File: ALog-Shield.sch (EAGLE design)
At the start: 25 parts, among them U1 DS3231MZ/V+T

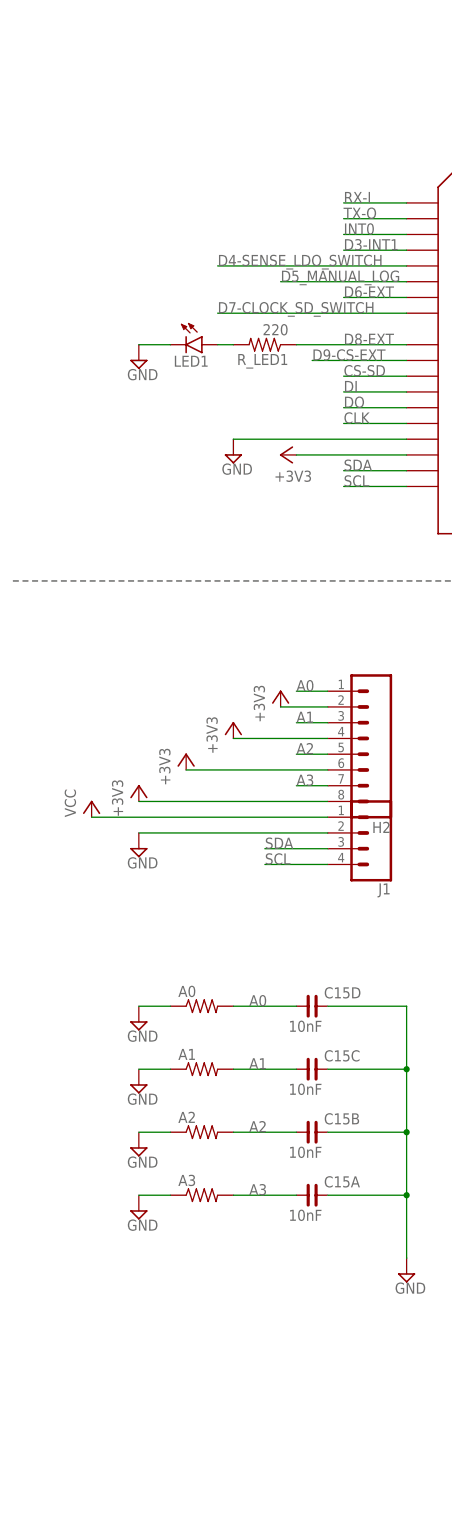
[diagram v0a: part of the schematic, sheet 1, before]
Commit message: ALog and Made in MN back silk
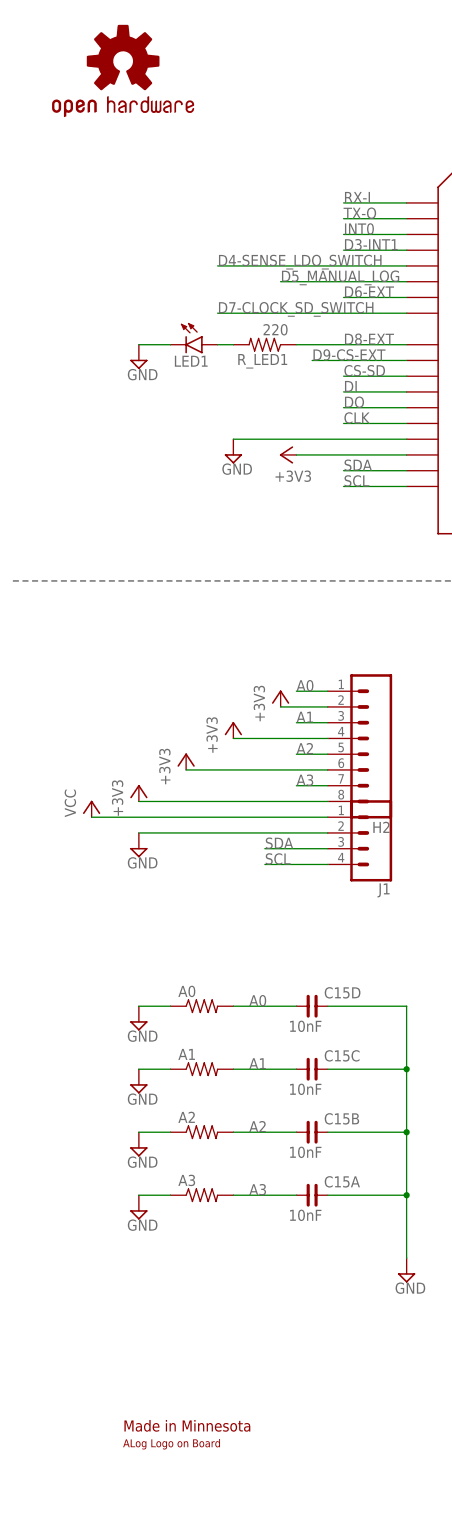
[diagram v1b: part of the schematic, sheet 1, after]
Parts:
- removed U$1: ALOG_LOGO_V1_5.5MM, awickert:ALOG_LOGO_V1_5.5MM
- removed U$4: NWLOGO, awickert:NWLOGO
- added LOGO1: OSHW-LOGOL, SparkFun-Aesthetics:OSHW-LOGOL
- added U$2: MADE_IN_MN_220_SHIELD, awickert:MADE_IN_MN_220_SHIELD
- added U$3: ALOG_LOG, awickert:ALOG_LOG
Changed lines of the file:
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@@
 <part name="SUPPLY45" library="supply2" deviceset="GND" device=""/>
 <part name="R_LED1" library="resistor" deviceset="R-US_" device="R0603" value="220"/>
-<part name="U$1" library="awickert" deviceset="ALOG_LOGO_V1_5.5MM" device=""/>
 <part name="+3V13" library="supply1" deviceset="+3V3" device=""/>
 <part name="A1" library="resistor" deviceset="R-US_" device="0207/10"/>
 <part name="SUPPLY47" library="supply2" deviceset="GND" device=""/>
-<part name="U$4" library="awickert" deviceset="NWLOGO" device=""/>
 <part name="LOGO2" library="SparkFun-Aesthetics" deviceset="OSHW-LOGO" device="M"/>
 <part name="SUPPLY52" library="supply2" deviceset="GND" device=""/>
@@
 <part name="C15" library="rc-master-smd" deviceset="CCA_" device="" value="10nF"/>
 <part name="CLOCK_BATT" library="awickert" deviceset="LINX-BAT-HLD-012-SMT-OTL" device="" value="Linx BAT-HLD-012-SMT"/>
+<part name="U$2" library="awickert" deviceset="MADE_IN_MN_220_SHIELD" device=""/>
+<part name="U$3" library="awickert" deviceset="ALOG_LOG" device=""/>
+<part name="LOGO1" library="SparkFun-Aesthetics" deviceset="OSHW-LOGO" device="L"/>
 </parts>
 <sheets>
@@
 <instance part="C15" gate="C" x="48.26" y="-175.26"/>
 <instance part="C15" gate="D" x="48.26" y="-165.1"/>
+<instance part="U$2" gate="G$1" x="17.78" y="-233.68"/>
+<instance part="U$3" gate="G$1" x="25.4" y="-236.22"/>
+<instance part="LOGO1" gate="G$1" x="17.78" y="-12.7"/>
 </instances>
 <busses>
@@
 <instance part="SUPPLY36" gate="GND" x="93.98" y="106.68"/>
 <instance part="SUPPLY41" gate="GND" x="58.42" y="233.68"/>
-<instance part="U$1" gate="G$1" x="127" y="53.34"/>
-<instance part="U$4" gate="G$1" x="127" y="55.88"/>
 <instance part="LOGO2" gate="G$1" x="165.1" y="60.96"/>
 <instance part="CLOCK_BATT_DECOUP" gate="G$1" x="99.06" y="129.54" smashed="yes">

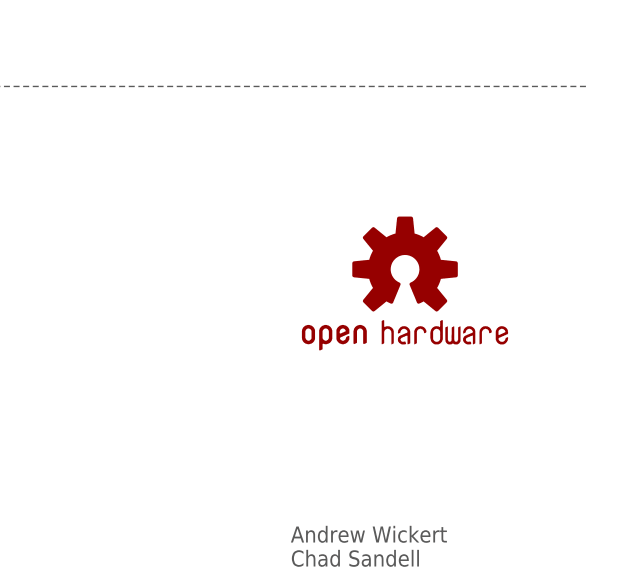
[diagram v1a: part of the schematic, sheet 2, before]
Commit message: Update silk and OSE logo
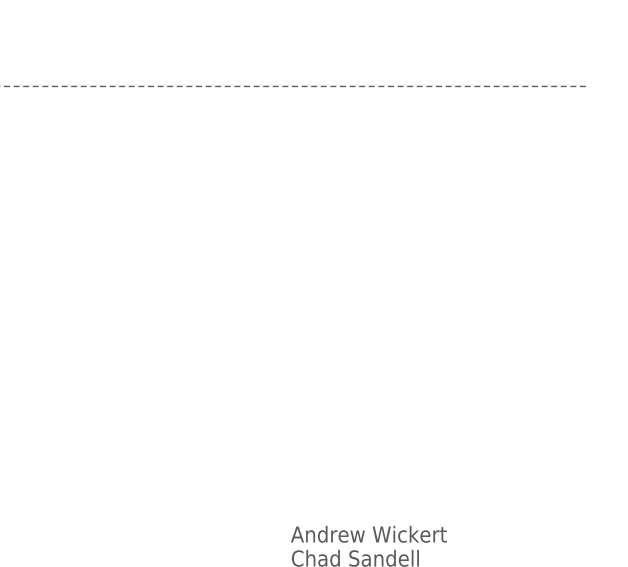
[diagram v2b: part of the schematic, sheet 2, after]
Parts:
- removed LOGO2: OSHW-LOGOM, SparkFun-Aesthetics:OSHW-LOGOM
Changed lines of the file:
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@@
 <part name="A1" library="resistor" deviceset="R-US_" device="0207/10"/>
 <part name="SUPPLY47" library="supply2" deviceset="GND" device=""/>
-<part name="LOGO2" library="SparkFun-Aesthetics" deviceset="OSHW-LOGO" device="M"/>
 <part name="SUPPLY52" library="supply2" deviceset="GND" device=""/>
 <part name="RESET" library="SparkFun-Electromechanical" deviceset="SWITCH-MOMENTARY-2" device="PTH" value="Reset"/>
@@
 <instance part="SUPPLY36" gate="GND" x="93.98" y="106.68"/>
 <instance part="SUPPLY41" gate="GND" x="58.42" y="233.68"/>
-<instance part="LOGO2" gate="G$1" x="165.1" y="60.96"/>
 <instance part="CLOCK_BATT_DECOUP" gate="G$1" x="99.06" y="129.54" smashed="yes">
 <attribute name="VALUE" x="100.584" y="124.841" size="1.778" layer="96"/>

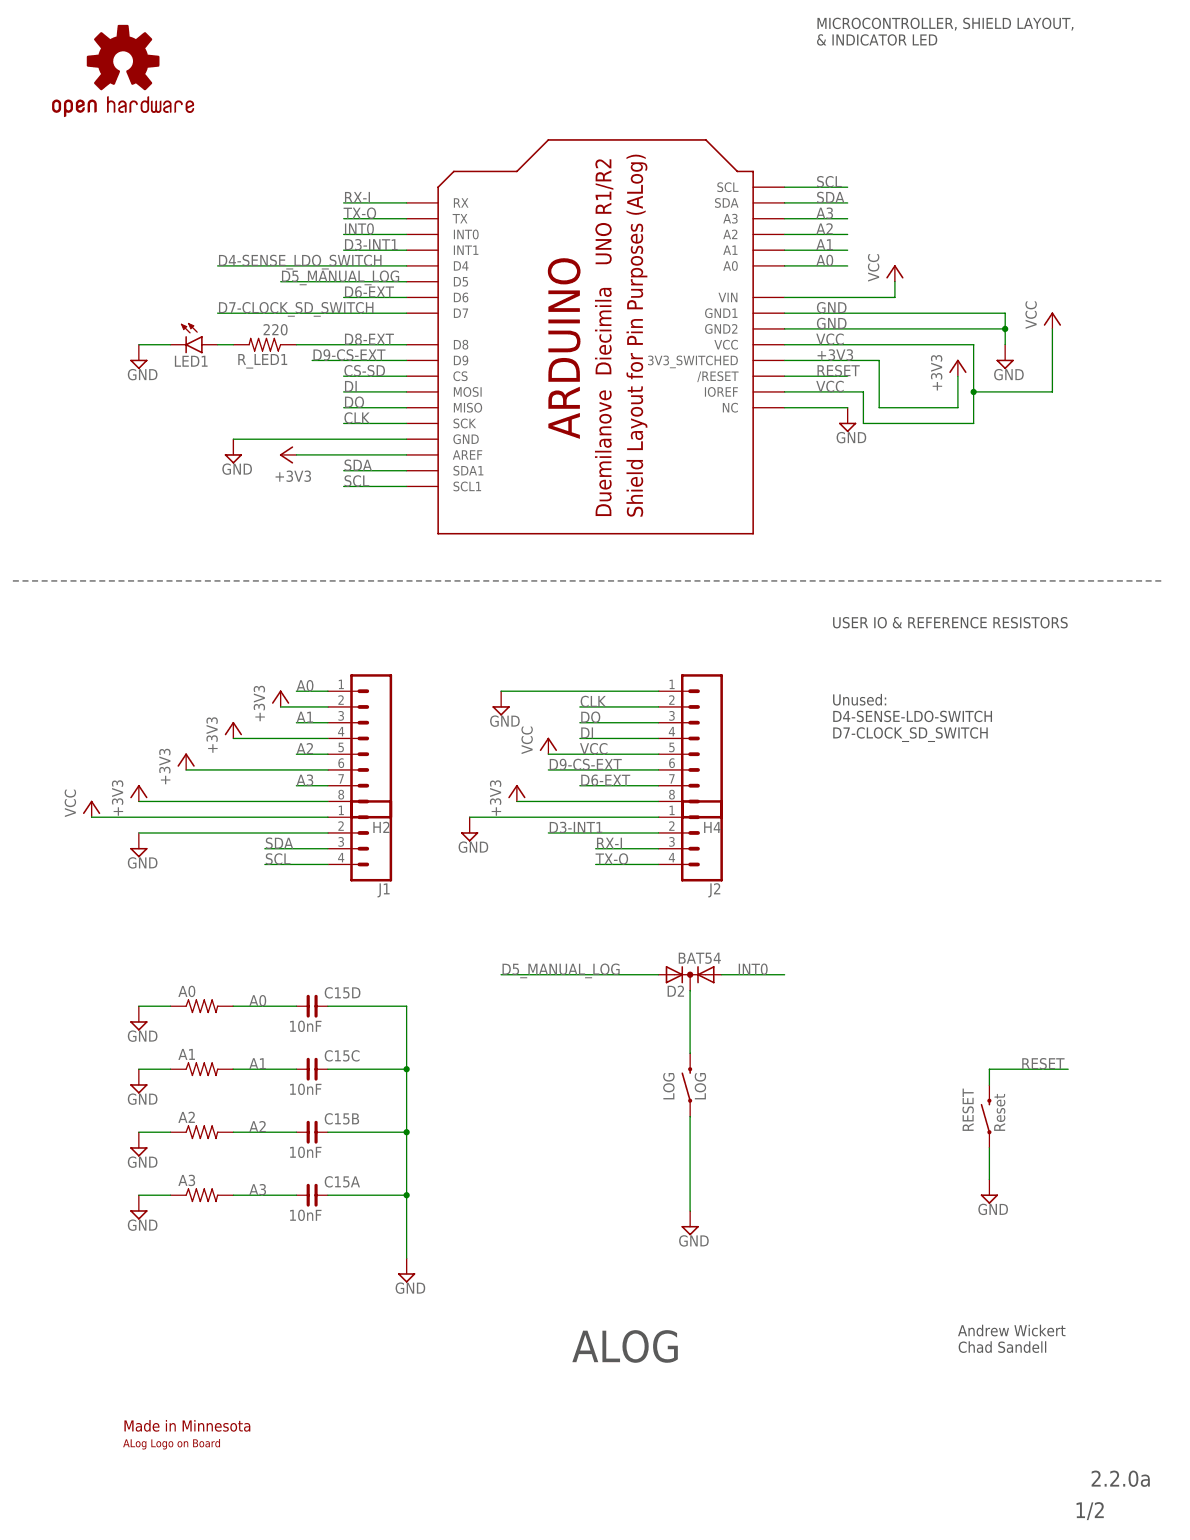
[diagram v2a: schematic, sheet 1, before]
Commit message: Added D4 and D7 out put points, will not populate with screw terminals
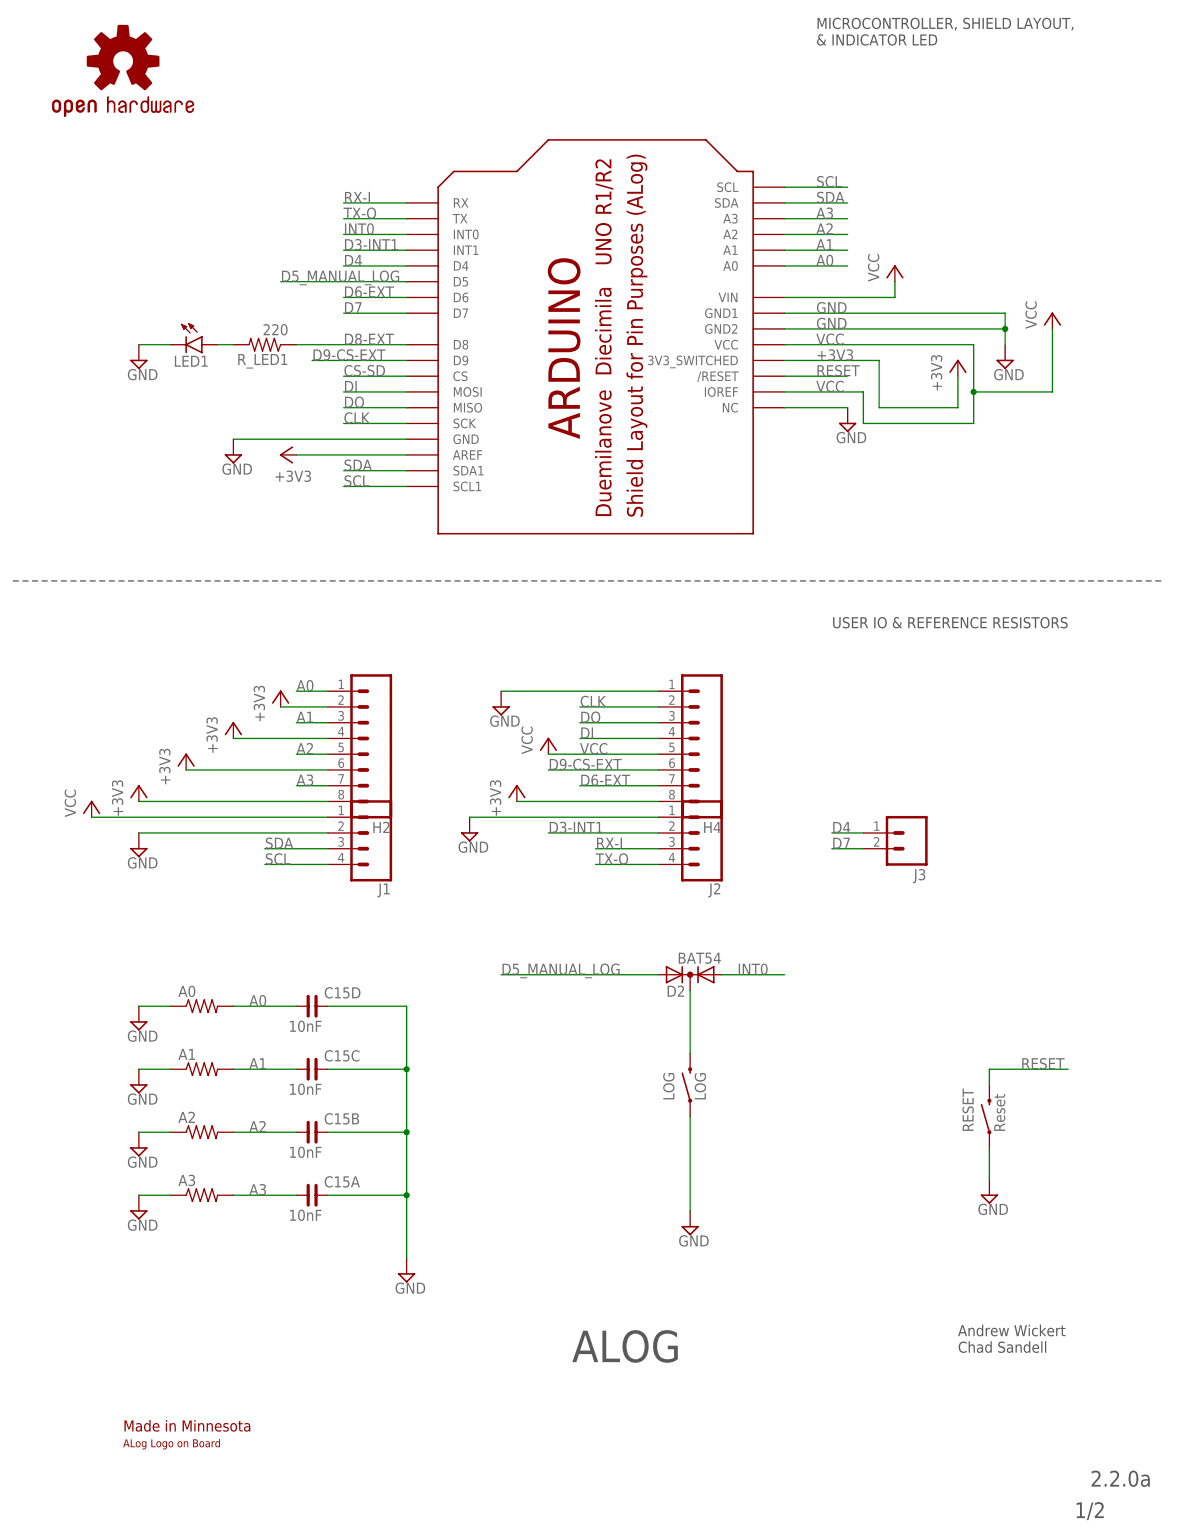
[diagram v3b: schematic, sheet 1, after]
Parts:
- added J3: (no value), SparkFun-Connectors:M023.5MM-NO_SILK
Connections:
- removed net D4-SENSE_LDO_SWITCH: U$9.D4
- removed net D7-CLOCK_SD_SWITCH: U$9.D7
- new net D4: J3.1, U$9.D4
- new net D7: J3.2, U$9.D7
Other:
- note removed: "Unused: D4-SENSE-LDO-SWITCH D7-CLOCK_SD_SWITCH"
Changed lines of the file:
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@@
 <part name="U$3" library="awickert" deviceset="ALOG_LOG" device=""/>
 <part name="LOGO1" library="SparkFun-Aesthetics" deviceset="OSHW-LOGO" device="L"/>
+<part name="J3" library="SparkFun-Connectors" deviceset="M02" device="3.5MM-NO_SILK"/>
 </parts>
 <sheets>
@@
 <text x="173.736" y="-242.57" size="2.54" layer="97">2.2.0a</text>
 <text x="171.196" y="-247.65" size="2.54" layer="97">1/2</text>
-<text x="132.08" y="-121.92" size="1.778" layer="97">Unused:
-D4-SENSE-LDO-SWITCH
-D7-CLOCK_SD_SWITCH</text>
 <text x="152.4" y="-220.98" size="1.778" layer="97">Andrew Wickert
 Chad Sandell</text>
@@
 <instance part="U$3" gate="G$1" x="25.4" y="-236.22"/>
 <instance part="LOGO1" gate="G$1" x="17.78" y="-12.7"/>
+<instance part="J3" gate="G$1" x="144.78" y="-137.16" rot="R180"/>
 </instances>
 <busses>
@@
 </segment>
 </net>
-<net name="D4-SENSE_LDO_SWITCH" class="0">
-<segment>
-<wire x1="33.02" y1="-45.72" x2="63.5" y2="-45.72" width="0.1524" layer="91"/>
+<net name="D4" class="0">
+<segment>
+<wire x1="53.34" y1="-45.72" x2="63.5" y2="-45.72" width="0.1524" layer="91"/>
 <pinref part="U$9" gate="G$1" pin="D4"/>
-<label x="33.02" y="-45.72" size="1.778" layer="95"/>
+<label x="53.34" y="-45.72" size="1.778" layer="95"/>
+</segment>
+<segment>
+<pinref part="J3" gate="G$1" pin="1"/>
+<wire x1="137.16" y1="-137.16" x2="132.08" y2="-137.16" width="0.1524" layer="91"/>
+<label x="132.08" y="-137.16" size="1.778" layer="95"/>
 </segment>
 </net>
@@
 </segment>
 </net>
-<net name="D7-CLOCK_SD_SWITCH" class="0">
-<segment>
-<wire x1="33.02" y1="-53.34" x2="63.5" y2="-53.34" width="0.1524" layer="91"/>
+<net name="D7" class="0">
+<segment>
+<wire x1="53.34" y1="-53.34" x2="63.5" y2="-53.34" width="0.1524" layer="91"/>
 <pinref part="U$9" gate="G$1" pin="D7"/>
-<label x="33.02" y="-53.34" size="1.778" layer="95"/>
-</segment>
-</net>
+<label x="53.34" y="-53.34" size="1.778" layer="95"/>
+</segment>
+<segment>
+<pinref part="J3" gate="G$1" pin="2"/>
+<wire x1="137.16" y1="-139.7" x2="132.08" y2="-139.7" width="0.1524" layer="91"/>
+<label x="132.08" y="-139.7" size="1.778" layer="95"/>
+</segment>
+</net>

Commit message: screw terminal + spacing to text
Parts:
- J3: device SparkFun-Connectors:M023.5MM-NO_SILK -> SparkFun-Connectors:M023.5MM
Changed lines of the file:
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@@
 <?xml version="1.0" encoding="utf-8"?>
 <!DOCTYPE eagle SYSTEM "eagle.dtd">
-<eagle version="7.7.0">
+<eagle version="8.3.1">
 <drawing>
 <settings>
 <setting alwaysvectorfont="yes"/>
+<setting keepoldvectorfont="yes"/>
 <setting verticaltext="up"/>
 </settings>
@@
 <part name="U$3" library="awickert" deviceset="ALOG_LOG" device=""/>
 <part name="LOGO1" library="SparkFun-Aesthetics" deviceset="OSHW-LOGO" device="L"/>
-<part name="J3" library="SparkFun-Connectors" deviceset="M02" device="3.5MM-NO_SILK"/>
+<part name="J3" library="SparkFun-Connectors" deviceset="M02" device="3.5MM"/>
 </parts>
 <sheets>
